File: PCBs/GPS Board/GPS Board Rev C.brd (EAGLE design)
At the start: 4 parts

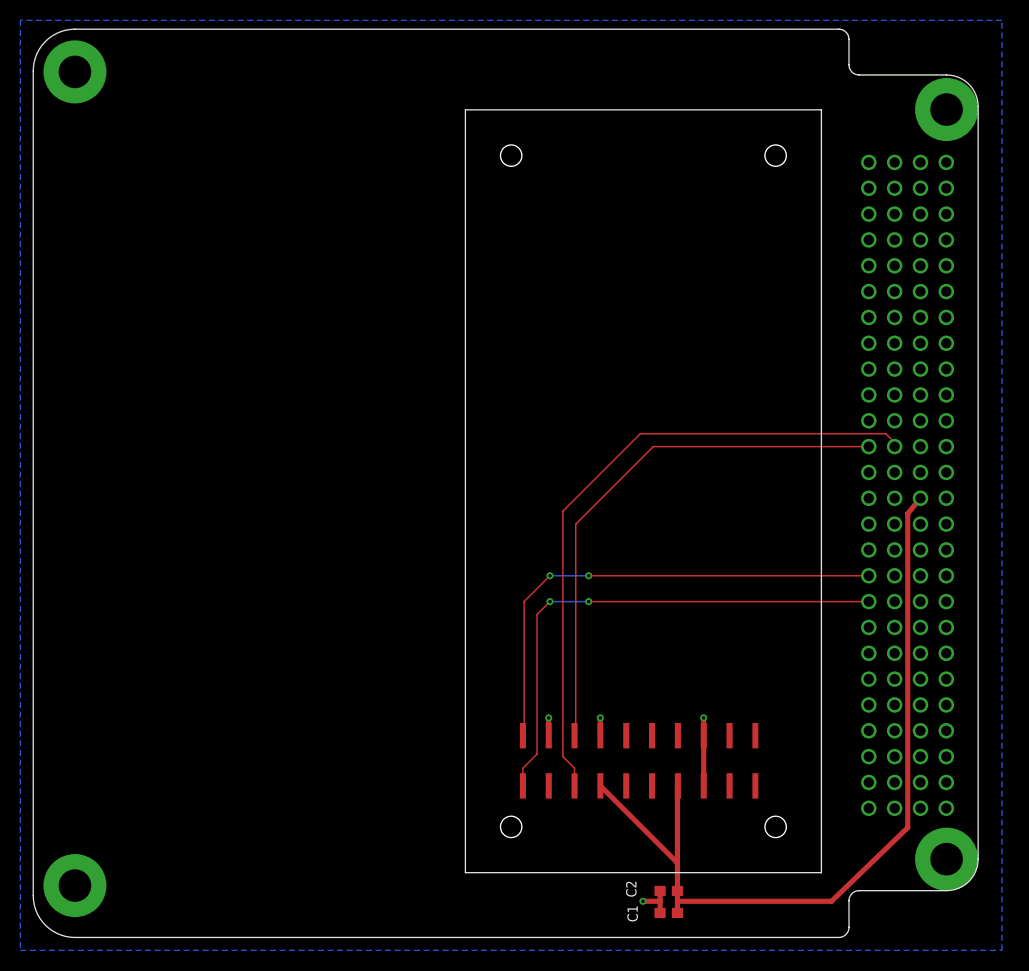
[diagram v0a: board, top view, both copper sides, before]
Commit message: Changed GPS power source to an EPS PDM, tweaked trace width
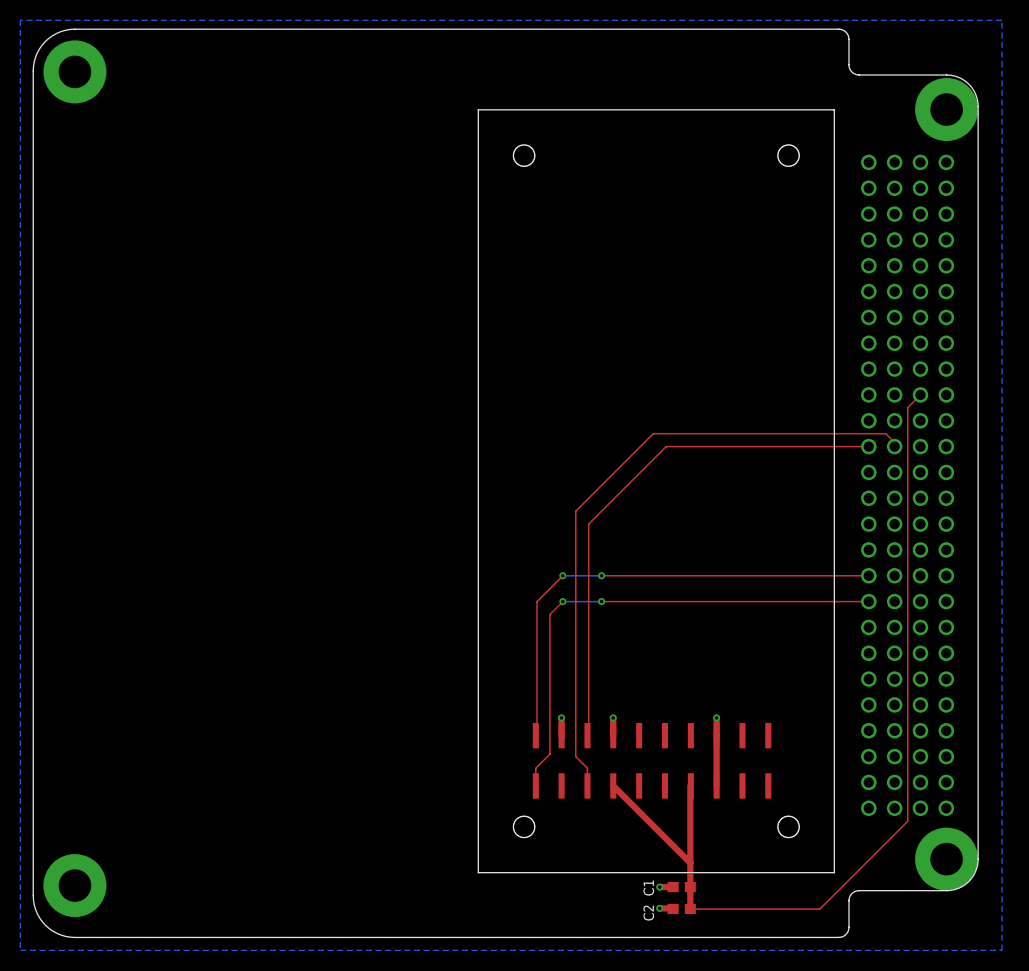
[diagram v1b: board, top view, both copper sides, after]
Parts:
- moved C1 2.84 mm to (63.8, 6.22)
- moved C2 2.18 mm to (63.8, 4.06)
- moved U$1 1.27 mm to (61.0, 45.7)
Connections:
- removed net VDD: C1.1, C2.1, U$1.14, U$1.8, U$2.P$79
- new net SW9: C1.1, C2.1, U$1.14, U$1.8, U$2.P$71
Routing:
- net SW9: track 0.00 -> 90.2 mm
- net VDD: track 81.6 -> 0.00 mm
- net VPP: track 52.8 -> 51.5 mm
- net TX: track 48.2 -> 46.9 mm
- net RX: track 50.6 -> 49.3 mm
- net PF: track 64.0 -> 62.8 mm
- net GND: track 14.8 -> 13.6 mm, vias 4 -> 5

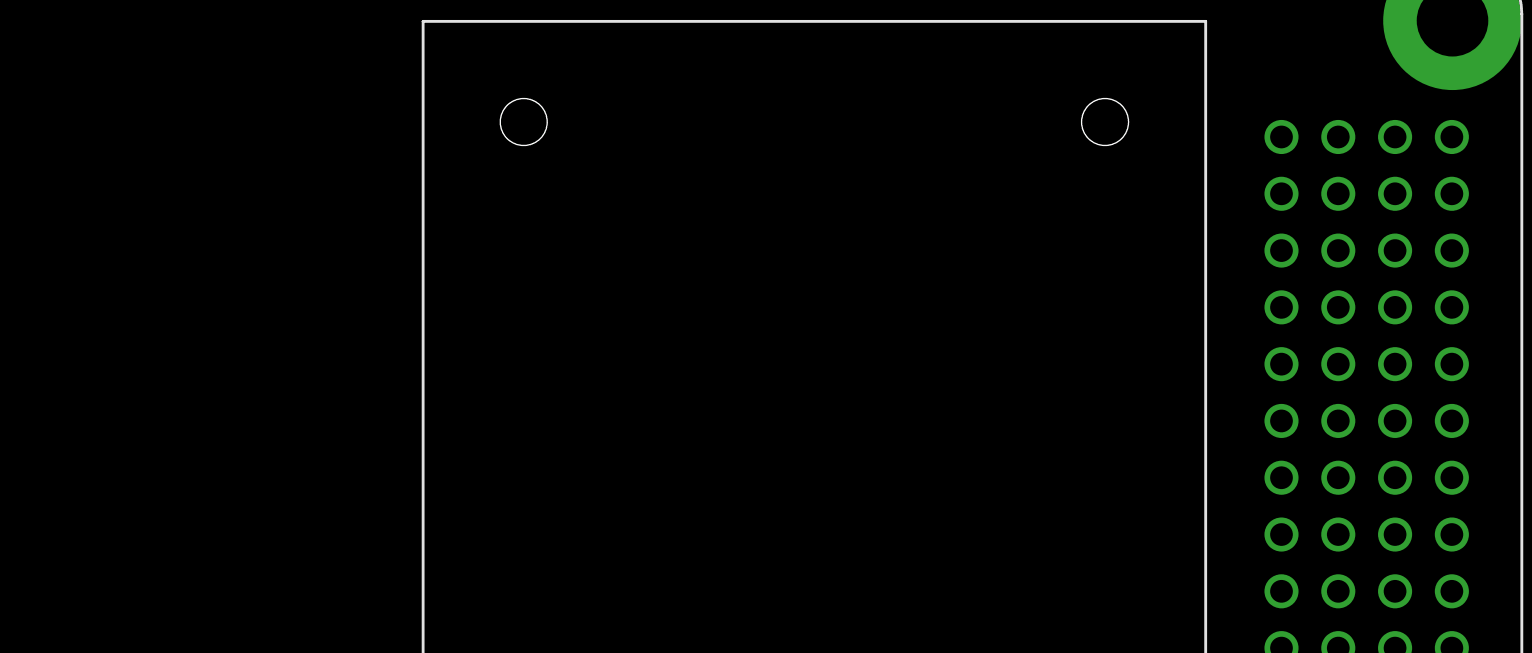
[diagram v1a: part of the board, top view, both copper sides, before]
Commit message: Add temp sensors to GPS and Radio boards
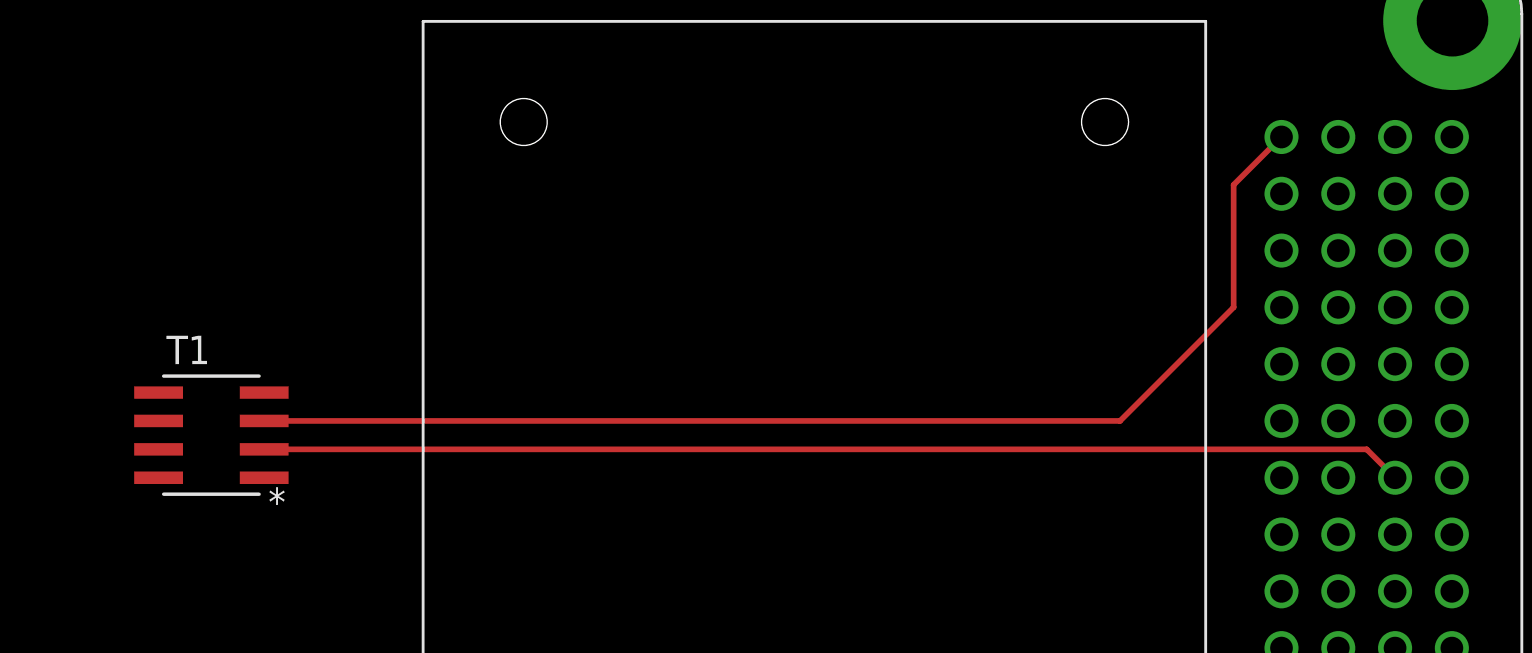
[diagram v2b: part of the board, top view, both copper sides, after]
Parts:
- added T1: AD590KRZ, AD590KRZ:R_8
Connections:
- new net N$1: T1.3, U$2.P$1
- new net SW5: T1.2, U$2.P$65
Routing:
- net N$1: track 0.00 -> 54.0 mm
- net SW5: track 0.00 -> 51.1 mm
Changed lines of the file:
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@@
 <layer number="56" name="wert" color="7" fill="1" visible="no" active="no"/>
 <layer number="57" name="tCAD" color="7" fill="1" visible="no" active="no"/>
+<layer number="88" name="SimResults" color="9" fill="1" visible="no" active="no"/>
+<layer number="89" name="SimProbes" color="9" fill="1" visible="no" active="no"/>
 <layer number="90" name="Modules" color="5" fill="1" visible="no" active="no"/>
 <layer number="91" name="Nets" color="2" fill="1" visible="no" active="no"/>
@@
 <attribute name="VALUE" x="58.928" y="7.239" size="0.635" layer="27" rot="R270"/>
 </element>
+<element name="T1" library="AD590KRZ" package="R_8" value="AD590KRZ" x="34.29" y="64.135" smashed="yes" rot="R180">
+<attribute name="MANUFACTURER_PART_NUMBER" value="AD590KRZ" x="34.29" y="64.135" size="1.778" layer="27" rot="R180" display="off"/>
+<attribute name="NAME" x="32.2834" y="67.31" size="1.27" layer="25" ratio="6" rot="SR0"/>
+<attribute name="VENDOR" value="Analog Devices" x="34.29" y="64.135" size="1.778" layer="27" rot="R180" display="off"/>
+</element>
 </elements>
 <signals>
@@
 <wire x1="55.88" y1="34.29" x2="82.15121875" y2="34.29" width="0.1524" layer="1"/>
 </signal>
+<signal name="SW5">
+<contactref element="U$2" pad="P$65"/>
+<contactref element="T1" pad="2"/>
+<wire x1="87.23121875" y1="62.23" x2="85.96121875" y2="63.5" width="0.254" layer="1"/>
+<wire x1="85.96121875" y1="63.5" x2="36.6522" y2="63.5" width="0.254" layer="1"/>
+</signal>
+<signal name="N$1">
+<contactref element="T1" pad="3"/>
+<contactref element="U$2" pad="P$1"/>
+<wire x1="36.6522" y1="64.77" x2="74.93" y2="64.77" width="0.254" layer="1"/>
+<wire x1="74.93" y1="64.77" x2="80.01" y2="69.85" width="0.254" layer="1"/>
+<wire x1="80.01" y1="69.85" x2="80.01" y2="75.32878125" width="0.254" layer="1"/>
+<wire x1="80.01" y1="75.32878125" x2="82.15121875" y2="77.47" width="0.254" layer="1"/>
+</signal>
 </signals>

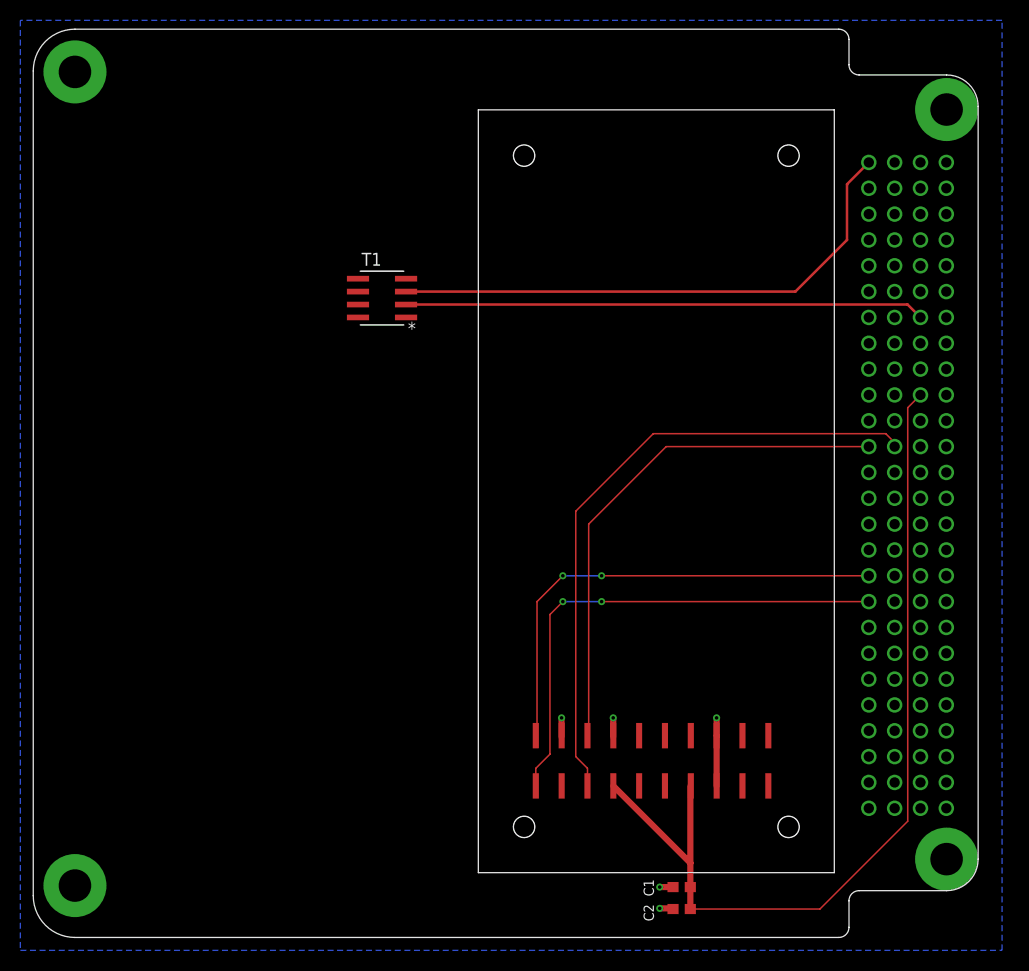
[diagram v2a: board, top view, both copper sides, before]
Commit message: Rotated GPS, bumped cap to 10uF
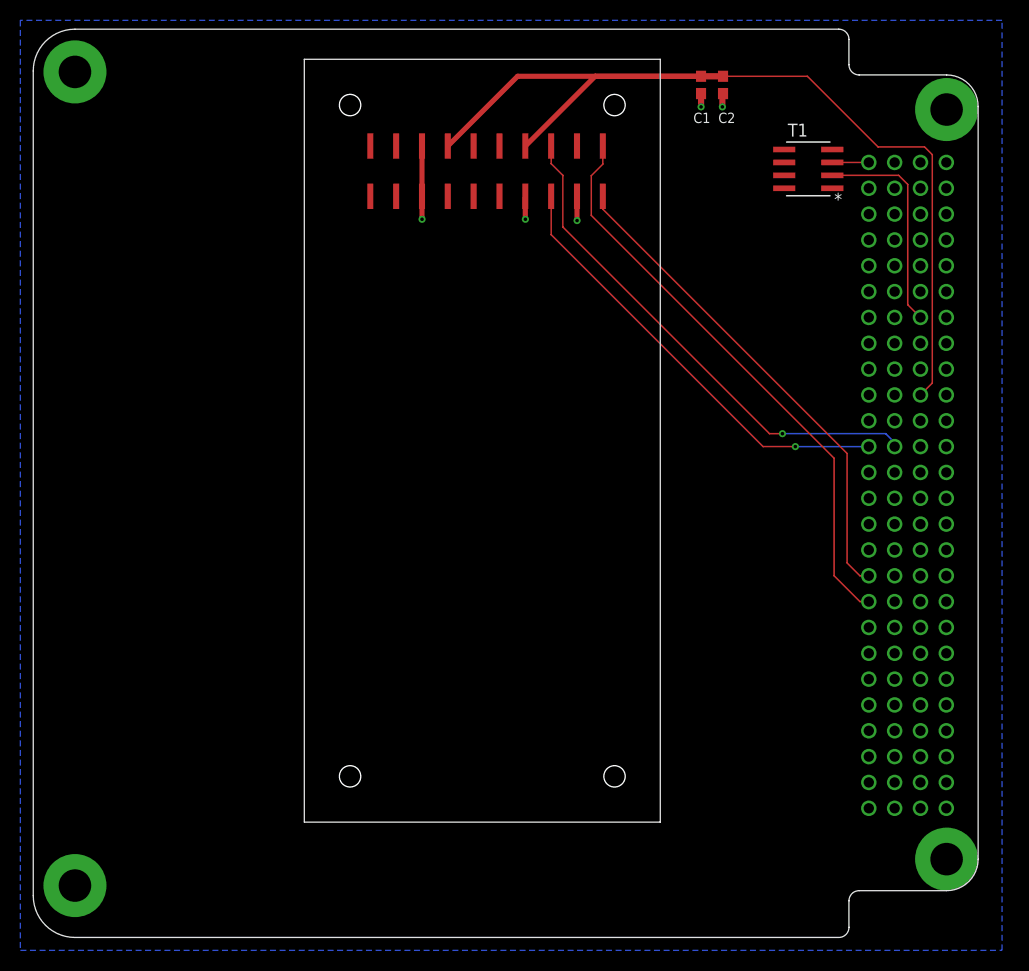
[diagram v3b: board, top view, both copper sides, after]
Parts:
- C2: value 1uF -> 10uF
- moved C2 81.1 mm to (67.8, 85.1), turned to 270 degrees
- moved C1 78.9 mm to (65.7, 85.1), turned to 270 degrees
- moved T1 43.8 mm to (76.2, 76.8)
- moved U$1 16.9 mm to (44.5, 49.5), turned to 90 degrees
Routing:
- net N$1: track 54.0 -> 3.59 mm
- net SW5: track 51.1 -> 21.4 mm
- net PF: track 62.8 -> 50.2 mm, vias 0 -> 1
- net VPP: track 51.5 -> 43.6 mm, vias 0 -> 1
- net RX: track 49.3 -> 57.1 mm, vias 2 -> 0
- net SW9: track 90.2 -> 97.9 mm
- net TX: track 46.9 -> 48.7 mm, vias 2 -> 0
- net GND: track 13.6 -> 14.8 mm

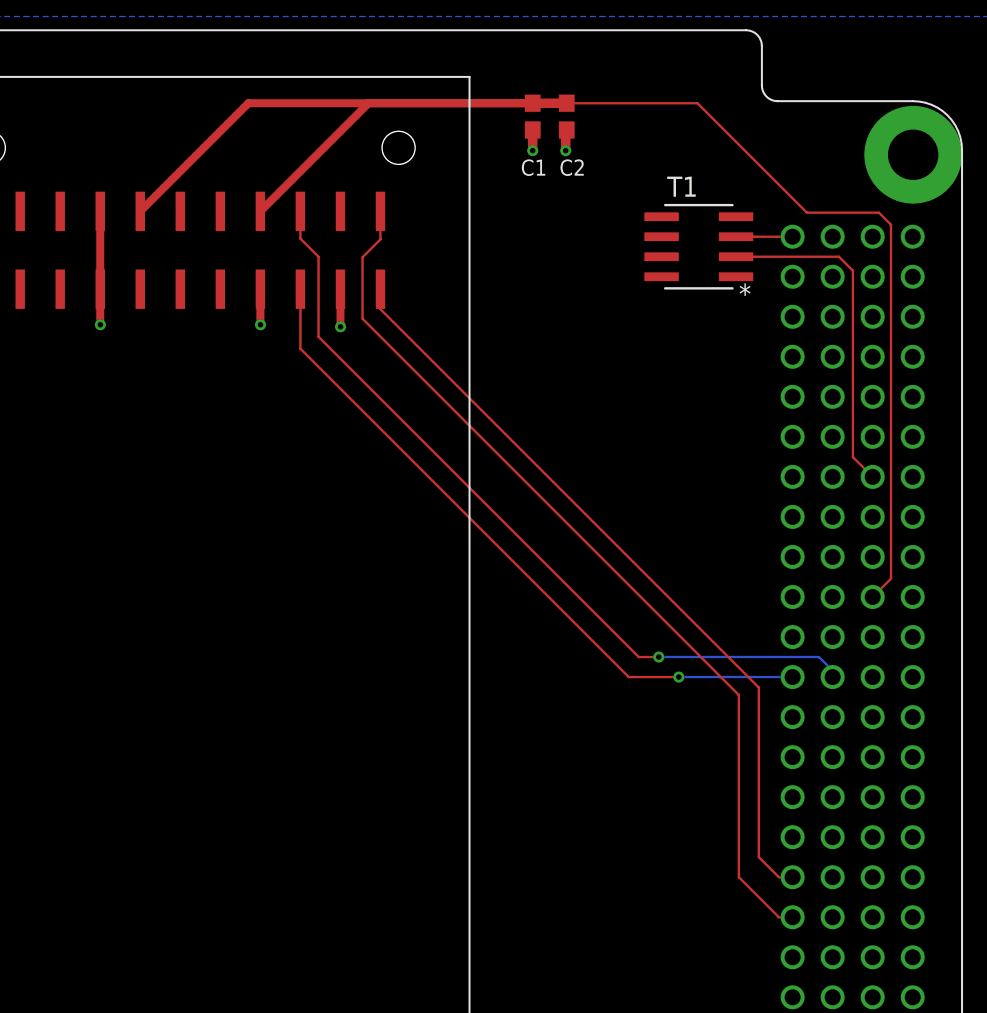
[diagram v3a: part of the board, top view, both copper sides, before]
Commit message: Remove temp sensors, tweak trace width
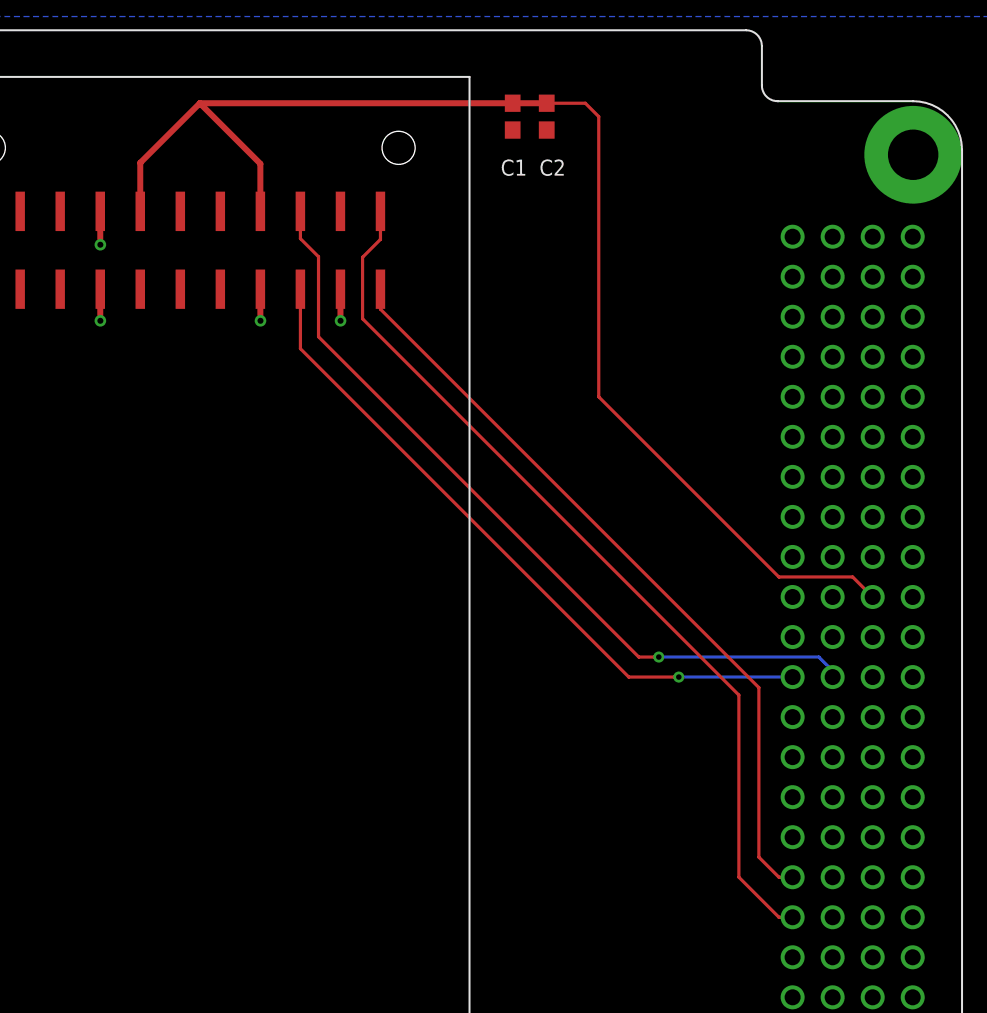
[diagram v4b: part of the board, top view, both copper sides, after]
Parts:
- removed T1: AD590KRZ, AD590KRZ:R_8
- C2: value 10uF -> 1uF
- moved C1 1.27 mm to (64.4, 85.1)
- moved C2 1.27 mm to (66.5, 85.1)
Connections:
- removed net N$1: T1.3, U$2.P$1
- net SW5: no longer T1.2
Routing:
- net SW5: track 21.4 -> 0.00 mm
- net SW9: track 97.9 -> 83.0 mm
- net GND: track 14.8 -> 8.52 mm, vias 5 -> 4
- net N$1: track 3.59 -> 0.00 mm
